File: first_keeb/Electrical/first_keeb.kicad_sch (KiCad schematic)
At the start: 5 parts, among them U1 Pico, U2 LM4040DBZ-3

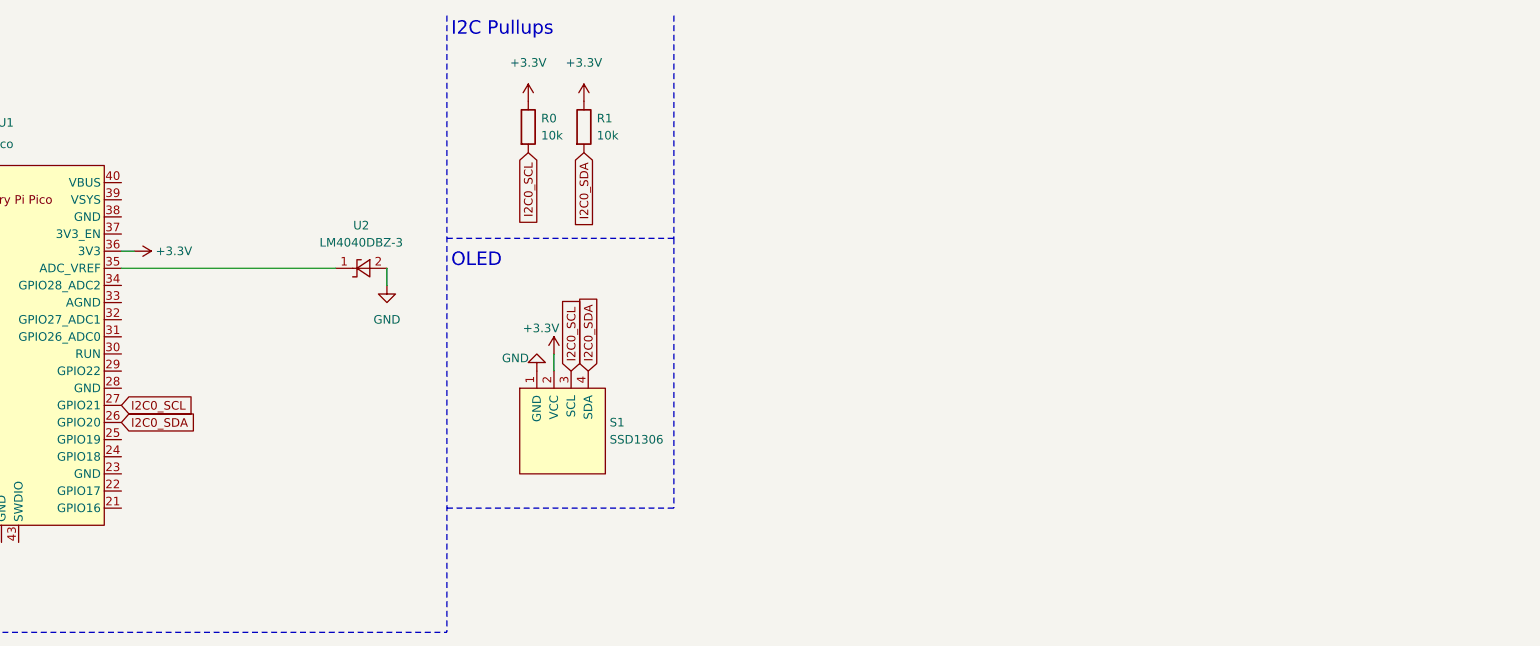
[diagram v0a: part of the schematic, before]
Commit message: adds jumper configuration to select any voltage source for testing purposes
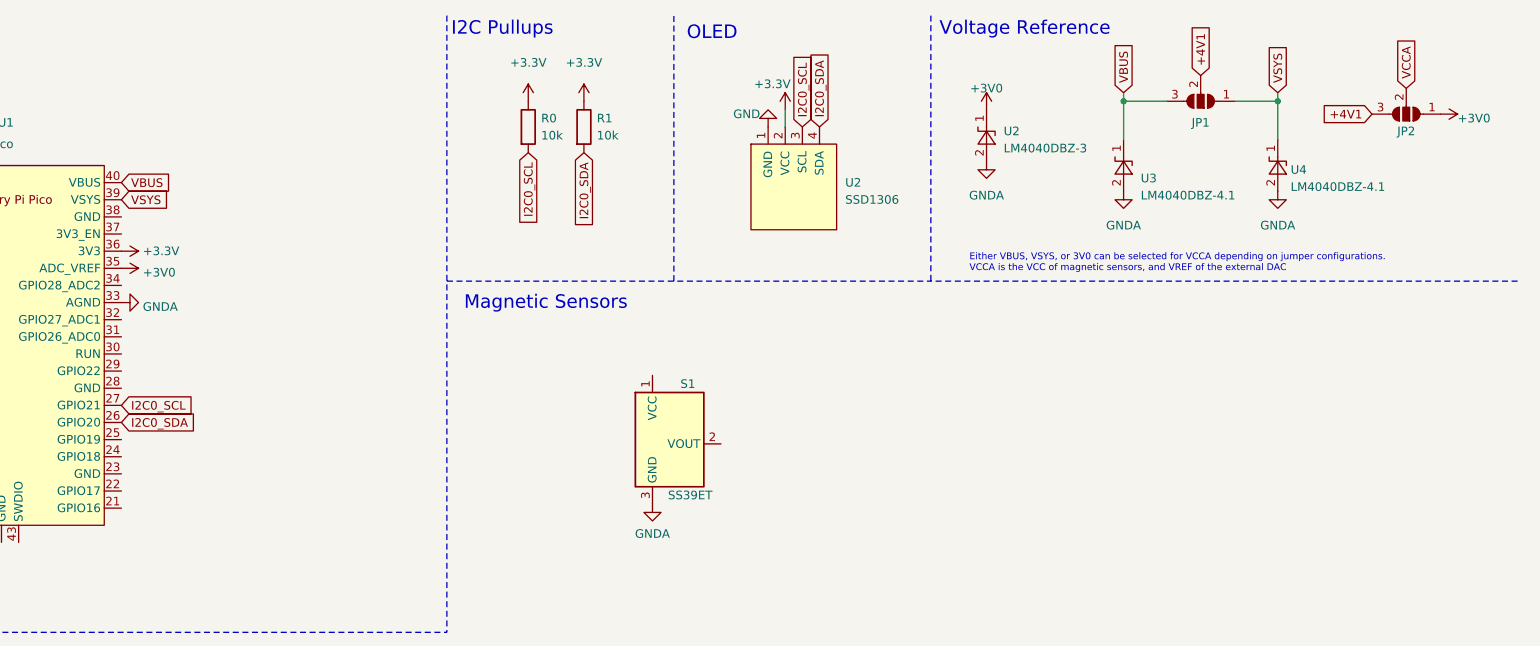
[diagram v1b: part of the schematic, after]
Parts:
- added JP1: Jumper, symbol Jumper:SolderJumper_3_Open
- added JP2: SolderJumper_3_Open, symbol Jumper:SolderJumper_3_Open
- added S1: SS39ET, Package_TO_SOT_SMD:SOT-23, symbol Sensor_Magnetic:SS39ET
- added U3, U4: LM4040DBZ-4.1, Package_TO_SOT_SMD:SOT-23, symbol Reference_Voltage:LM4040DBZ-4.1
- renumbered S1 to U2
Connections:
- net GND: no longer U2.2 (A)
- net GNDA: now reaches U1.33 (AGND)
- net GNDA: now also U2.2 (A), S1.3 (GND), U3.2 (A), U4.2 (A)
- net +3V0: now reaches U1.35 (ADC_VREF), U2.1 (K)
- net +3V0: now also JP2.1 (A)
- net VSYS: now reaches U1.39 (VSYS)
- net VSYS: now also JP1.1 (A), U4.1 (K)
- net VBUS: now reaches U1.40 (VBUS)
- net VBUS: now also JP1.3 (B), U3.1 (K)
- new net +4V1: JP1.2 (C), JP2.3 (B)
- new net VCCA: JP2.2 (C)
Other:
- note added: "Either VBUS, VSYS, or 3V0 can be selected for VCCA depending on jumper configurations. VCCA is the VCC of magnetic sensors, and VREF of the external DAC"
- note added: "Magnetic Sensors"
- note added: "Voltage Reference"
- moved on the sheet: U2

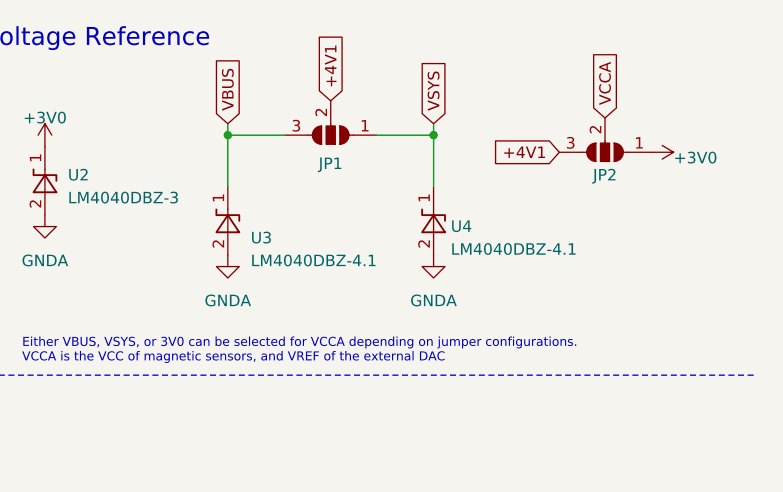
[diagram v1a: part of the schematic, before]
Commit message: improve jumper config circuit
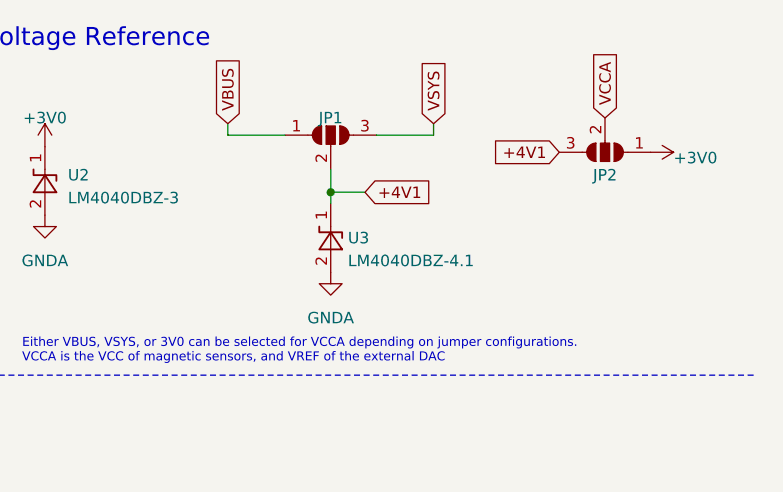
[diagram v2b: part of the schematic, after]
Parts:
- removed U4: LM4040DBZ-4.1, Package_TO_SOT_SMD:SOT-23, symbol Reference_Voltage:LM4040DBZ-4.1
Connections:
- net +4V1: now also U3.1 (K)
- net VBUS: now also JP1.1 (A); no longer JP1.3 (B), U3.1 (K)
- net VSYS: now also JP1.3 (B); no longer JP1.1 (A)
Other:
- moved on the sheet: JP1, U3
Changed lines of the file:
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@@
 (kicad_sch (version 20230121) (generator eeschema)
   (paper "A4")
-  (junction (at 226.695 24.765) (diameter 0) (color 0 0 0 0)
-  )
-  (junction (at 249.555 24.765) (diameter 0) (color 0 0 0 0)
+  (junction (at 238.125 31.115) (diameter 0) (color 0 0 0 0)
   )
   (wire (pts (xy 243.205 24.765) (xy 249.555 24.765))
@@
     (stroke (width 0) (type default))
   )
-  (wire (pts (xy 249.555 24.765) (xy 249.555 30.48))
+  (wire (pts (xy 238.125 31.115) (xy 238.125 32.385))
     (stroke (width 0) (type default))
   )
@@
     (stroke (width 0) (type default))
   )
-  (wire (pts (xy 226.695 24.765) (xy 226.695 30.48))
-    (stroke (width 0) (type default))
-  )
   (polyline (pts (xy 198.12 12.065) (xy 198.12 51.435))
     (stroke (width 0) (type dash))
@@
     (stroke (width 0) (type default))
   )
+  (wire (pts (xy 241.935 31.115) (xy 238.125 31.115))
+    (stroke (width 0) (type default))
+  )
   (polyline (pts (xy 126.365 51.435) (xy 198.12 51.435))
     (stroke (width 0) (type dash))
   )
+  (wire (pts (xy 238.125 28.575) (xy 238.125 31.115))
+    (stroke (width 0) (type default))
+  )
   (polyline (pts (xy 285.115 51.435) (xy 198.12 51.435))
     (stroke (width 0) (type dash))
@@
     (effects (font (size 2 2)) (justify left bottom))
   )
-  (global_label "+4V1" (shape input) (at 238.125 20.955 90) (fields_autoplaced)
+  (global_label "+4V1" (shape input) (at 241.935 31.115 0) (fields_autoplaced)
     (effects (font (size 1.27 1.27)) (justify left))
-    (property "Intersheetrefs" "${INTERSHEET_REFS}" (at 238.125 12.9692 90)
+    (property "Intersheetrefs" "${INTERSHEET_REFS}" (at 249.9208 31.115 0)
       (effects (font (size 1.27 1.27)) (justify left) hide)
     )
@@
     )
   )
-  (symbol (lib_id "power:GNDA") (at 226.695 38.1 0) (unit 1)
+  (symbol (lib_id "power:GNDA") (at 238.125 40.005 0) (unit 1)
     (in_bom yes) (on_board yes) (dnp no) (fields_autoplaced)
-    (property "Reference" "#PWR06" (at 226.695 44.45 0)
+    (property "Reference" "#PWR06" (at 238.125 46.355 0)
       (effects (font (size 1.27 1.27)) hide)
     )
-    (property "Value" "GNDA" (at 226.695 43.18 0)
+    (property "Value" "GNDA" (at 238.125 45.085 0)
       (effects (font (size 1.27 1.27)))
     )
-    (property "Footprint" "" (at 226.695 38.1 0)
+    (property "Footprint" "" (at 238.125 40.005 0)
       (effects (font (size 1.27 1.27)) hide)
     )
-    (property "Datasheet" "" (at 226.695 38.1 0)
+    (property "Datasheet" "" (at 238.125 40.005 0)
       (effects (font (size 1.27 1.27)) hide)
     )
@@
     )
   )
-  (symbol (lib_id "Reference_Voltage:LM4040DBZ-4.1") (at 226.695 34.29 90) (unit 1)
+  (symbol (lib_id "Reference_Voltage:LM4040DBZ-4.1") (at 238.125 36.195 90) (unit 1)
     (in_bom yes) (on_board yes) (dnp no)
-    (property "Reference" "U3" (at 229.235 36.195 90)
+    (property "Reference" "U3" (at 240.03 36.195 90)
       (effects (font (size 1.27 1.27)) (justify right))
     )
-    (property "Value" "LM4040DBZ-4.1" (at 229.235 38.735 90)
+    (property "Value" "LM4040DBZ-4.1" (at 240.03 38.735 90)
       (effects (font (size 1.27 1.27)) (justify right))
     )
-    (property "Footprint" "Package_TO_SOT_SMD:SOT-23" (at 231.775 34.29 0)
+    (property "Footprint" "Package_TO_SOT_SMD:SOT-23" (at 243.205 36.195 0)
       (effects (font (size 1.27 1.27) italic) hide)
     )
-    (property "Datasheet" "http://www.ti.com/lit/ds/symlink/lm4040-n.pdf" (at 226.695 34.29 0)
+    (property "Datasheet" "http://www.ti.com/lit/ds/symlink/lm4040-n.pdf" (at 238.125 36.195 0)
       (effects (font (size 1.27 1.27) italic) hide)
     )
@@
     )
   )
-  (symbol (lib_id "power:GNDA") (at 249.555 38.1 0) (unit 1)
-    (in_bom yes) (on_board yes) (dnp no) (fields_autoplaced)
-    (property "Reference" "#PWR08" (at 249.555 44.45 0)
-      (effects (font (size 1.27 1.27)) hide)
-    )
-    (property "Value" "GNDA" (at 249.555 43.18 0)
-      (effects (font (size 1.27 1.27)))
-    )
-    (property "Footprint" "" (at 249.555 38.1 0)
-      (effects (font (size 1.27 1.27)) hide)
-    )
-    (property "Datasheet" "" (at 249.555 38.1 0)
-      (effects (font (size 1.27 1.27)) hide)
-    )
-    (pin "1")
-    (instances
-      (project "first_keeb"
-        (path "/e63e39d7-6ac0-4ffd-8aa3-1841a4541b55"
-          (reference "#PWR08") (unit 1)
-        )
-      )
-    )
-  )
   (symbol (lib_id "power:+3.3V") (at 176.53 26.035 0) (unit 1)
     (in_bom yes) (on_board yes) (dnp no)
@@
     )
   )
-  (symbol (lib_id "Reference_Voltage:LM4040DBZ-4.1") (at 249.555 34.29 90) (unit 1)
-    (in_bom yes) (on_board yes) (dnp no)
-    (property "Reference" "U4" (at 251.46 34.925 90)
-      (effects (font (size 1.27 1.27)) (justify right))
-    )
-    (property "Value" "LM4040DBZ-4.1" (at 251.46 37.465 90)
-      (effects (font (size 1.27 1.27)) (justify right))
-    )
-    (property "Footprint" "Package_TO_SOT_SMD:SOT-23" (at 254.635 34.29 0)
-      (effects (font (size 1.27 1.27) italic) hide)
-    )
-    (property "Datasheet" "http://www.ti.com/lit/ds/symlink/lm4040-n.pdf" (at 249.555 34.29 0)
-      (effects (font (size 1.27 1.27) italic) hide)
-    )
-    (pin "1")
-    (pin "2")
-    (instances
-      (project "first_keeb"
-        (path "/e63e39d7-6ac0-4ffd-8aa3-1841a4541b55"
-          (reference "U4") (unit 1)
-        )
-      )
-    )
-  )
-  (symbol (lib_id "Jumper:SolderJumper_3_Open") (at 238.125 24.765 180) (unit 1)
+  (symbol (lib_id "Jumper:SolderJumper_3_Open") (at 238.125 24.765 0) (unit 1)
     (in_bom yes) (on_board yes) (dnp no) (fields_autoplaced)
-    (property "Reference" "JP1" (at 238.125 27.94 0)
+    (property "Reference" "JP1" (at 238.125 22.86 0)
       (effects (font (size 1.27 1.27)))
     )
-    (property "Value" "Jumper" (at 238.125 30.48 0)
+    (property "Value" "Jumper" (at 238.125 19.05 0)
       (effects (font (size 1.27 1.27)) hide)
     )

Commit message: adds a lot of new things to schematic
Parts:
- removed JP1: Jumper, symbol Jumper:SolderJumper_3_Open
- added C1, C10, C11, C12, C13, C14, C15, C16, C17, C18, C19, C2, C20, C21, C22, C23, C24, C25, C26, C27, C28, C29, C3, C30, C5, C6, C7, C8, C9: 1uF, symbol Device:C_Small
- added C4: 10uF, symbol Device:C_Small
- added Cx: xF, symbol Device:C_Small
- added D1, D10, D11, D12, D13, D14, D15, D16, D17, D18, D19, D2, D20, D21, D22, D23, D24, D3, D4, D5, D6, D7, D8, D9: WS2812B, LED_SMD:LED_WS2812B_PLCC4_5.0x5.0mm_P3.2mm, symbol LED:WS2812B
- added R2: 300R, symbol Device:R
- added R3: 1k, symbol Device:R
- added R4: 10k, symbol Device:R
- added S10, S11, S12, S13, S14, S15, S16, S17, S18, S2, S3, S4, S5, S6, S7, S8, S9: SS39ET, Package_TO_SOT_SMD:SOT-23, symbol Sensor_Magnetic:SS39ET
- added SW1: SW_Push, symbol Switch:SW_Push
- added SW3: RotaryEncoder_Switch, symbol Device:RotaryEncoder_Switch
- added U4, U5: MCP3008, symbol Analog_ADC:MCP3008
- U2: value LM4040DBZ-3 -> LM4040-3
- U3: value LM4040DBZ-4.1 -> LM4040-4.1
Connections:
- net VBUS is gone; now on net VSYS: U1.40 (VBUS)
- net +3V0: now also JP2.3 (B); no longer JP2.1 (A)
- net GND: now also U1.13 (GND), U1.18 (GND), U1.23 (GND), U1.28 (GND), U1.3 (GND), U1.38 (GND), U1.8 (GND), C10.2, C11.2, C12.2, C13.2, C14.2, C15.2, C16.2, C17.2, C18.2, C19.2, C20.2, C21.2, C22.2, C23.2, C24.2, C25.2, C26.2, C27.2, C28.2, C29.2, C30.2, C4.2, C7.2, C8.2, C9.2, D1.3 (VSS), D10.3 (VSS), D11.3 (VSS), D12.3 (VSS), D13.3 (VSS), D14.3 (VSS), D15.3 (VSS), D16.3 (VSS), D17.3 (VSS), D18.3 (VSS), D19.3 (VSS), D2.3 (VSS), D20.3 (VSS), D21.3 (VSS), D22.3 (VSS), D23.3 (VSS), D24.3 (VSS), D3.3 (VSS), D4.3 (VSS), D5.3 (VSS), D6.3 (VSS), D7.3 (VSS), D8.3 (VSS), D9.3 (VSS), SW1.2, SW3.S2, U4.9 (DGND), U5.9 (DGND)
- net GNDA: now also C1.2, C2.2, C3.2, C5.2, C6.2, Cx.2, S10.3 (GND), S11.3 (GND), S12.3 (GND), S13.3 (GND), S14.3 (GND), S15.3 (GND), S16.3 (GND), S17.3 (GND), S18.3 (GND), S2.3 (GND), S3.3 (GND), S4.3 (GND), S5.3 (GND), S6.3 (GND), S7.3 (GND), S8.3 (GND), S9.3 (GND), U4.14 (AGND), U5.14 (AGND)
- net VCCA: now also C3.1, C5.1, C6.1, U4.15 (Vref), U5.15 (Vref)
- net VSYS: now also S1.1 (VCC), C1.1, C10.1, C11.1, C12.1, C13.1, C14.1, C15.1, C16.1, C17.1, C18.1, C19.1, C2.1, C20.1, C21.1, C22.1, C23.1, C24.1, C25.1, C26.1, C27.1, C28.1, C29.1, C30.1, C4.1, C7.1, C8.1, C9.1, Cx.1, D1.1 (VDD), D10.1 (VDD), D11.1 (VDD), D12.1 (VDD), D13.1 (VDD), D14.1 (VDD), D15.1 (VDD), D16.1 (VDD), D17.1 (VDD), D18.1 (VDD), D19.1 (VDD), D2.1 (VDD), D20.1 (VDD), D21.1 (VDD), D22.1 (VDD), D23.1 (VDD), D24.1 (VDD), D3.1 (VDD), D4.1 (VDD), D5.1 (VDD), D6.1 (VDD), D7.1 (VDD), D8.1 (VDD), D9.1 (VDD), R3.1, S10.1 (VCC), S11.1 (VCC), S12.1 (VCC), S13.1 (VCC), S14.1 (VCC), S15.1 (VCC), S16.1 (VCC), S17.1 (VCC), S18.1 (VCC), S2.1 (VCC), S3.1 (VCC), S4.1 (VCC), S5.1 (VCC), S6.1 (VCC), S7.1 (VCC), S8.1 (VCC), S9.1 (VCC), U4.16 (Vdd), U5.16 (Vdd)
- net ROT0_SW0: now reaches U1.11 (GPIO8)
- net ROT0_SW1: now reaches U1.12 (GPIO9)
- net ROT0_D0: now reaches U1.14 (GPIO10)
- net ROT0_D1: now reaches U1.15 (GPIO11)
- net ROT1_D0: now reaches U1.16 (GPIO12)
- net ROT1_D1: now reaches U1.17 (GPIO13)
- net ROT1_SW0: now reaches U1.19 (GPIO14)
- net ROT1_SW1: now reaches U1.20 (GPIO15)
- net SW1: now reaches U1.21 (GPIO16)
- net SW1: now also R4.2, SW1.1
- net SW2: now reaches U1.22 (GPIO17)
- net BACK_LED_D: now reaches U1.24 (GPIO18)
- net BACK_LED_D: now also D13.4 (DIN)
- net SW_LED_D: now reaches U1.25 (GPIO19)
- net SW_LED_D: now also D1.4 (DIN)
- net at U1.29 (GPIO22): now also R2.2
- net at U1.30 (RUN): now also R2.1
- net RPI_ADC0: now reaches U1.31 (GPIO26_ADC0)
- net RPI_ADC0: now also S1.2 (VOUT)
- net RPI_ADC1: now reaches U1.32 (GPIO27_ADC1)
- net RPI_ADC1: now also S2.2 (VOUT)
- net SPI0_SCK: now reaches U1.4 (GPIO2)
- net SPI0_SCK: now also U4.13 (CLK), U5.13 (CLK)
- net SPI0_MOSI: now reaches U1.5 (GPIO3)
- net SPI0_MOSI: now also U4.11 (Din), U5.11 (Din)
- net SPI0_MISO: now reaches U1.6 (GPIO4)
- net SPI0_MISO: now also U4.12 (Dout), U5.12 (Dout)
- net SPI0_CS0n: now reaches U1.7 (GPIO5)
- net SPI0_CS0n: now also U4.10 (~{CS}/SHDN), U5.10 (~{CS}/SHDN)
- net SPI0_CS1n: now reaches U1.9 (GPIO6)
- net +4V1 renamed 4V1
- net 4V1: now also JP2.1 (A), R3.2; no longer JP2.3 (B)
- new net: D22.2 (DOUT), D23.4 (DIN)
- new net: D21.2 (DOUT), D22.4 (DIN)
- new net: D1.2 (DOUT), D2.4 (DIN)
- new net: D8.2 (DOUT), D9.4 (DIN)
- new net: D7.2 (DOUT), D8.4 (DIN)
- new net: D17.2 (DOUT), D18.4 (DIN)
- new net: D16.2 (DOUT), D17.4 (DIN)
- new net: D6.2 (DOUT), D7.4 (DIN)
- new net: D5.2 (DOUT), D6.4 (DIN)
- new net: D3.2 (DOUT), D4.4 (DIN)
- new net: D2.2 (DOUT), D3.4 (DIN)
- new net: D13.2 (DOUT), D14.4 (DIN)
- new net: D15.2 (DOUT), D16.4 (DIN)
- new net: D23.2 (DOUT), D24.4 (DIN)
- new net: D10.2 (DOUT), D11.4 (DIN)
- new net: D10.4 (DIN), D9.2 (DOUT)
- new net: D11.2 (DOUT), D12.4 (DIN)
- new net: D20.2 (DOUT), D21.4 (DIN)
- new net: D19.2 (DOUT), D20.4 (DIN)
- new net: D18.2 (DOUT), D19.4 (DIN)
- new net: D14.2 (DOUT), D15.4 (DIN)
- new net: D4.2 (DOUT), D5.4 (DIN)
- new net ADC0: S3.2 (VOUT), U4.1 (CH0)
- new net ADC1: S4.2 (VOUT), U4.2 (CH1)
- new net ADC10: S10.2 (VOUT), U5.3 (CH2)
- new net ADC11: S11.2 (VOUT), U5.4 (CH3)
- new net ADC12: S12.2 (VOUT), U5.5 (CH4)
- new net ADC13: S13.2 (VOUT), U5.6 (CH5)
- new net ADC14: S14.2 (VOUT), U5.7 (CH6)
- new net ADC15: S15.2 (VOUT), U5.8 (CH7)
- new net ADC2: S17.2 (VOUT), U4.3 (CH2)
- new net ADC3: S18.2 (VOUT), U4.4 (CH3)
- new net ADC4: S16.2 (VOUT), U4.5 (CH4)
- new net ADC5: S5.2 (VOUT), U4.6 (CH5)
- new net ADC6: S6.2 (VOUT), U4.7 (CH6)
- new net ADC7: S7.2 (VOUT), U4.8 (CH7)
- new net ADC8: S8.2 (VOUT), U5.1 (CH0)
- new net ADC9: S9.2 (VOUT), U5.2 (CH1)
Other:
- note added: ""R_s must be small enough to supply the minimum I_z required for operation of the regulator, as given by data-sheet parameters. At the other extreme, maximum V_s and minimum I_l, R_s must be large enough to limit I_z to less than its maximum-rated value of 15 mA." I_load_2 = 2*I_ref_MCP3008 = 2*70uA = 0.140mA I_load_1 = 0.070mA R_min = (V_s_max - V_z)/(I_load + I_z_max) = (5.25V - 4.096V)/(0.140m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"
- note added: "ADC"
- note added: "Backlight LEDs"
- note added: "Buttons"
- note added: "Capacitor values from MCP3008 datasheet."
- note added: "Either 4V1, or 3V0 can be selected for VCCA depending on jumper configurations. VCCA is VCC of magnetic sensors, and VREF of the external ADC. Capacitor value from MCP3008 datasheet."
- note added: "From Pico datasheet: "If the USB port is the only power source, VSYS and VBUS can be safely shorted together to eliminate the Schottky diode drop (which improves efficiency and reduces ripple on VSYS)."
- note added: "GPIO22 connected to RUN pin so that reset can be asserted programatically. Capacitor values from MCP3008 datasheet."
- note added: "Represents the decoupling cap that will be added to VCC on every sensor. xF represents a nondetermined value of these capacitors. As of right now, they will most likely be 1uF or 0.1uF. May also need to add LC or RC circuit to filter out high noise if the decoupling capacitor is not enough."
- note added: "Rotary Encoders"
- note added: "Switch LEDs"
- note added: "The sensors require too much supply current for them to be connected to VCCA. If using VSYS proves to be unnaceptable, more voltage references will be used to accomodate these sensors."
- note removed: "Either VBUS, VSYS, or 3V0 can be selected for VCCA depending on jumper configurations. VCCA is the VCC of magnetic sensors, and VREF of the external DAC"
- title: (none) -> End Game Prototyping Board
- moved on the sheet: JP2, S1, U2, U3

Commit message: ready to start frist pcb
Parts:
- removed R4: 10k, symbol Device:R
- added Cx1: xF, symbol Device:C_Small
- added JP1: SolderJumper_3_Open, symbol Jumper:SolderJumper_3_Open
- added R10, R7, R8, R9: 0, symbol Device:R
- added R5, R6: 10k, symbol Device:R
- added SW2: SW_Push, symbol Switch:SW_Push
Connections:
- net +3V3: now also JP1.3 (B), R5.1, R6.1
- net GND: now also SW2.2
- net GNDA: now also Cx1.2
- net ROT0_D0: now also U1.4 (GPIO2); no longer U1.14 (GPIO10)
- net ROT0_D1: now also U1.5 (GPIO3); no longer U1.15 (GPIO11)
- net ROT0_SW0: now also U1.6 (GPIO4); no longer U1.11 (GPIO8)
- net ROT0_SW1: now also U1.7 (GPIO5); no longer U1.12 (GPIO9)
- net ROT1_D0: now also U1.9 (GPIO6); no longer U1.16 (GPIO12)
- net ROT1_D1: now also U1.10 (GPIO7); no longer U1.17 (GPIO13)
- net ROT1_SW0: now also U1.11 (GPIO8); no longer U1.19 (GPIO14)
- net ROT1_SW1: now also U1.12 (GPIO9); no longer U1.20 (GPIO15)
- net SPI0_CS0n: now also U1.17 (GPIO13), R5.2; no longer U1.7 (GPIO5), U5.10 (~{CS}/SHDN)
- net SPI0_CS1n: now also U1.19 (GPIO14), U5.10 (~{CS}/SHDN), R6.2; no longer U1.9 (GPIO6)
- net SPI0_MISO: now also U1.16 (GPIO12), R7.1, R8.1; no longer U1.6 (GPIO4), U4.12 (Dout), U5.12 (Dout)
- net SPI0_MOSI: now also R10.2; no longer U1.5 (GPIO3)
- net SPI0_SCK: now also R9.1; no longer U1.4 (GPIO2)
- net SW2: now also SW2.1
- net VSYS: now also JP1.1 (A); no longer S1.1 (VCC), S10.1 (VCC), S11.1 (VCC), S12.1 (VCC), S13.1 (VCC), S14.1 (VCC), S15.1 (VCC), S16.1 (VCC), S17.1 (VCC), S18.1 (VCC), S2.1 (VCC), S3.1 (VCC), S4.1 (VCC), S5.1 (VCC), S6.1 (VCC), S7.1 (VCC), S8.1 (VCC), S9.1 (VCC)
- new net: R9.2, U1.14 (GPIO10)
- new net: R8.2, U5.12 (Dout)
- new net: R7.2, U4.12 (Dout)
- new net: R10.1, U1.15 (GPIO11)
- new net ADCx: Cx1.1
- new net VCC: JP1.2 (C), S1.1 (VCC), S10.1 (VCC), S11.1 (VCC), S12.1 (VCC), S13.1 (VCC), S14.1 (VCC), S15.1 (VCC), S16.1 (VCC), S17.1 (VCC), S18.1 (VCC), S2.1 (VCC), S3.1 (VCC), S4.1 (VCC), S5.1 (VCC), S6.1 (VCC), S7.1 (VCC), S8.1 (VCC), S9.1 (VCC)
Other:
- note added: "Debounce buttons"
- note added: "Debounce buttons in software. Set internal pull up to high."
- note added: "Represents the decoupling cap that will be added to every sensor. xF represents a nondetermined value of these capacitors. As of right now, they will most likely be 1uF or 0.1uF. May also need to add LC or RC circuit to filter out high noise if the decoupling capacitor is not enough."
- note added: "SPI pullup for CS signals. Should not be needed, but just in case."
- note added: "SS39ET are optimized for low noise output, so it is expected that no output filtering is necessary."
- note removed: "Represents the decoupling cap that will be added to VCC on every sensor. xF represents a nondetermined value of these capacitors. As of right now, they will most likely be 1uF or 0.1uF. May also need to add LC or RC circuit to filter out high noise if the decoupling capacitor is not enough."
- moved on the sheet: C2, C6, SW1, SW3, U5
